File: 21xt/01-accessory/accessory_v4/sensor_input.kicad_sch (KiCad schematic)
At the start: 3 parts, among them J1 Conn_02x23_Counter_Clockwise, J2 Mezzanine Edge

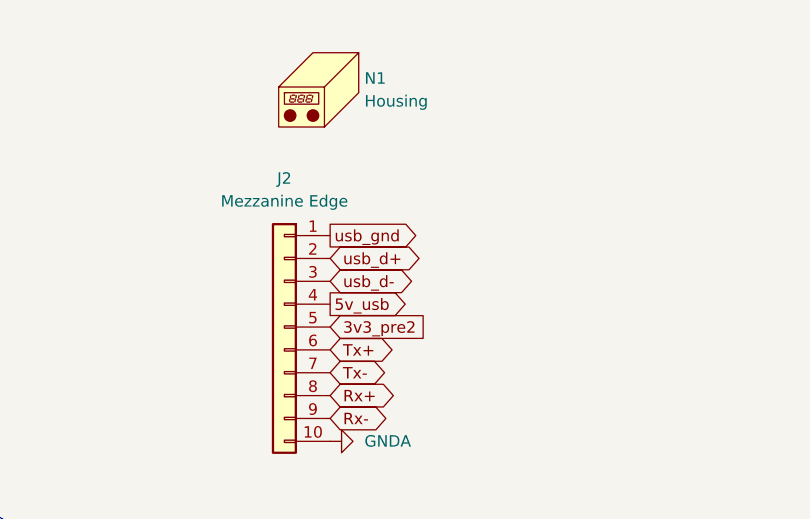
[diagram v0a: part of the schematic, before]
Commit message: Finished accessory & peripheral layout revisions
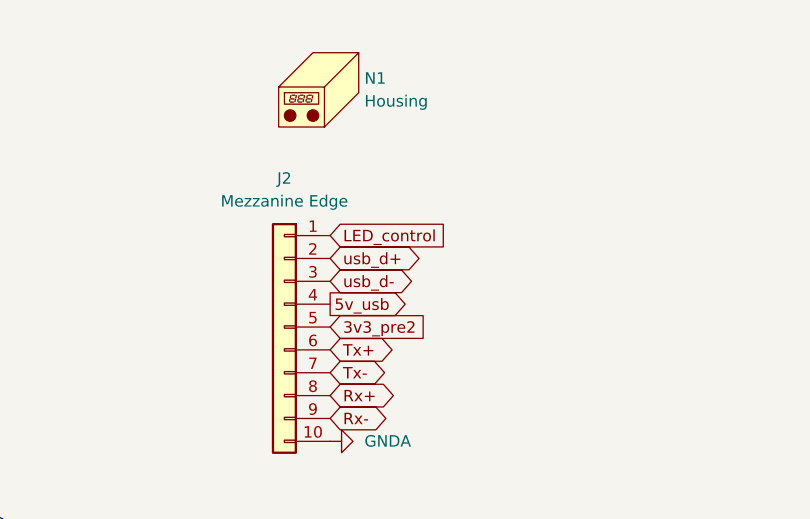
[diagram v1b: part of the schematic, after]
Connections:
- net usb_gnd renamed LED_control
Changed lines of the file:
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@@
 		)
 	)
-	(global_label "usb_gnd"
-		(shape output)
+	(global_label "LED_control"
+		(shape input)
 		(at 198.12 49.53 0)
 		(fields_autoplaced yes)
@@
 		)
 		(property "Intersheetrefs" "${INTERSHEET_REFS}"
-			(at 208.8459 49.53 0)
+			(at 212.2326 49.53 0)
 			(effects
 				(font

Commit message: finished accessory v4
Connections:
- net GNDA: now also J2.1 (Pin_1); no longer J2.10 (Pin_10)
- net LED_control: now also J2.10 (Pin_10); no longer J2.1 (Pin_1)
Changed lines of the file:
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@@
+		)
+	)
+	(global_label "LED_control"
+		(shape input)
+		(at 198.12 72.39 0)
+		(fields_autoplaced yes)
+		(effects
+			(font
+				(size 1.27 1.27)
+			)
+			(justify left)
+		)
+		(property "Intersheetrefs" "${INTERSHEET_REFS}"
+			(at 212.2326 72.39 0)
+			(effects
+				(font
+					(size 1.27 1.27)
+				)
+				(justify left)
+				(hide yes)
+			)
 		)
 	)
@@
 				)
 				(justify right)
-				(hide yes)
-			)
-		)
-	)
-	(global_label "LED_control"
-		(shape input)
-		(at 198.12 49.53 0)
-		(fields_autoplaced yes)
-		(effects
-			(font
-				(size 1.27 1.27)
-			)
-			(justify left)
-		)
-		(property "Intersheetrefs" "${INTERSHEET_REFS}"
-			(at 212.2326 49.53 0)
-			(effects
-				(font
-					(size 1.27 1.27)
-				)
-				(justify left)
 				(hide yes)
 			)
@@
 	)
 	(symbol
+		(lib_id "power:GNDA")
+		(at 198.12 49.53 90)
+		(unit 1)
+		(exclude_from_sim no)
+		(in_bom yes)
+		(on_board yes)
+		(dnp no)
+		(property "Reference" "#PWR01"
+			(at 204.47 49.53 0)
+			(effects
+				(font
+					(size 1.27 1.27)
+				)
+				(hide yes)
+			)
+		)
+		(property "Value" "GNDA"
+			(at 201.93 49.53 90)
+			(effects
+				(font
+					(size 1.27 1.27)
+				)
+				(justify right)
+			)
+		)
+		(property "Footprint" ""
+			(at 198.12 49.53 0)
+			(effects
+				(font
+					(size 1.27 1.27)
+				)
+				(hide yes)
+			)
+		)
+		(property "Datasheet" ""
+			(at 198.12 49.53 0)
+			(effects
+				(font
+					(size 1.27 1.27)
+				)
+				(hide yes)
+			)
+		)
+		(property "Description" ""
+			(at 198.12 49.53 0)
+			(effects
+				(font
+					(size 1.27 1.27)
+				)
+				(hide yes)
+			)
+		)
+		(pin "1"
+		)
+		(instances
+			(project "accessory_v4"
+				(path "/5dacc41e-ffff-47d3-9300-200c6018c603/67100f97-5262-4274-9380-0583de02d6bc"
+					(reference "#PWR01")
+					(unit 1)
+				)
+			)
+		)
+	)
+	(symbol
 		(lib_id "Connector_Generic:Conn_02x23_Counter_Clockwise")
 		(at 132.08 95.25 0)
@@
 					(unit 1)
 				)
-			)
-		)
-	)
-	(symbol
-		(lib_id "power:GNDA")
-		(at 198.12 72.39 90)
-		(unit 1)
-		(exclude_from_sim no)
-		(in_bom yes)
-		(on_board yes)
-		(dnp no)
-		(property "Reference" "#PWR01"
-			(at 204.47 72.39 0)
-			(effects
-				(font
-					(size 1.27 1.27)
-				)
-				(hide yes)
-			)
-		)
-		(property "Value" "GNDA"
-			(at 201.93 72.39 90)
-			(effects
-				(font
-					(size 1.27 1.27)
-				)
-				(justify right)
-			)
-		)
-		(property "Footprint" ""
-			(at 198.12 72.39 0)
-			(effects
-				(font
-					(size 1.27 1.27)
-				)
-				(hide yes)
-			)
-		)
-		(property "Datasheet" ""
-			(at 198.12 72.39 0)
-			(effects
-				(font
-					(size 1.27 1.27)
-				)
-				(hide yes)
-			)
-		)
-		(property "Description" ""
-			(at 198.12 72.39 0)
-			(effects
-				(font
-					(size 1.27 1.27)
-				)
-				(hide yes)
-			)
-		)
-		(pin "1"
-		)
-		(instances
-			(project "accessory_v3"
-				(path "/5dacc41e-ffff-47d3-9300-200c6018c603/67100f97-5262-4274-9380-0583de02d6bc"
-					(reference "#PWR01")
-					(unit 1)
-				)
